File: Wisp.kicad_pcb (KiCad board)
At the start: 4 copper layers, 36 x 36 mm, 38 parts, among them J1 USB4105-GF-A, J2 SM04B-GHS-TB, J3 Conn_01x05_Pin, J4 Conn_01x05_Pin, J5 Conn_01x04_Pin, J6 Conn_01x04_Pin, J9 Conn_02x04_Counter_Clockwise, SW2 PTS810 SJM 250 SMTR LFS, SW3 PTS810 SJM 250 SMTR LFS, U1 ESP32-S3-MINI-1, U2 USBLC6-2SC6, U3 AP2112K-3.3TRG1, U4 TPS7A2033PYCJR, U5 DWM3000TR13

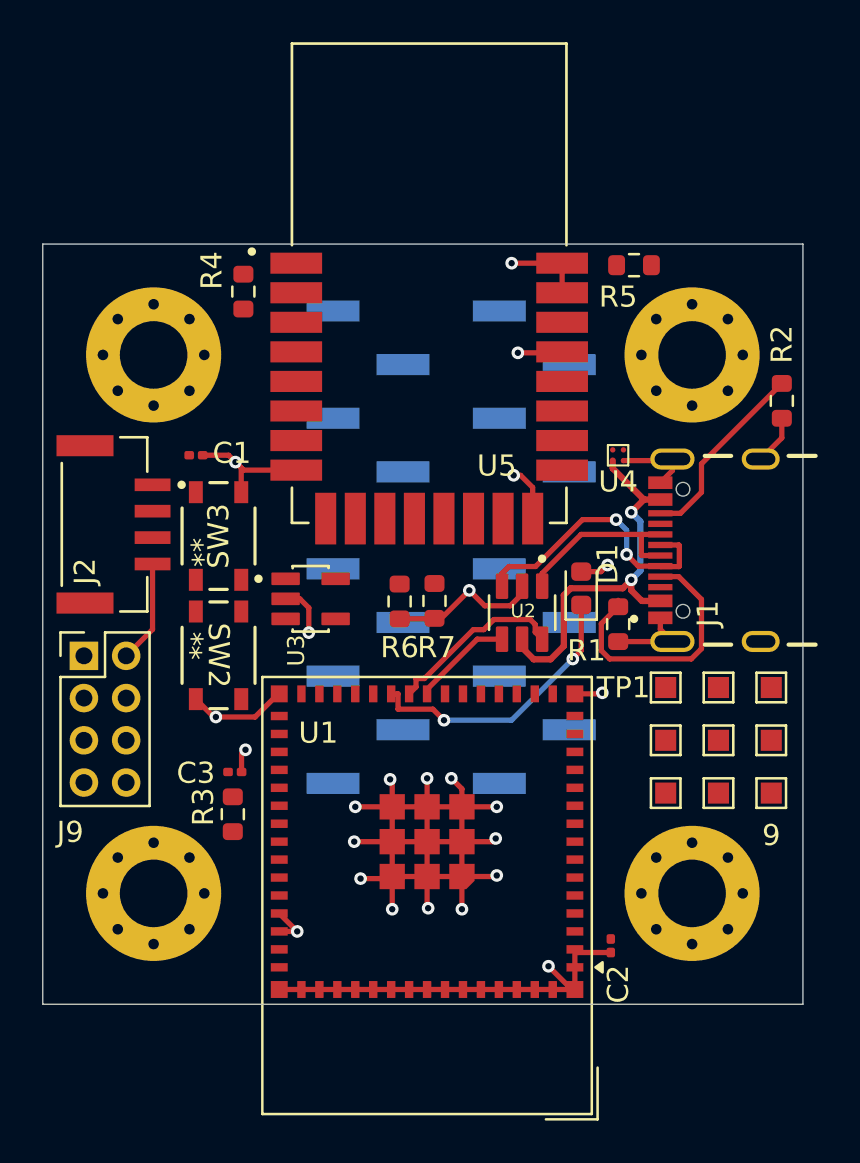
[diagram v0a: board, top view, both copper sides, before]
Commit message: Shifted to a 4 layer board, routed 75% of the traces. DRC needs to run
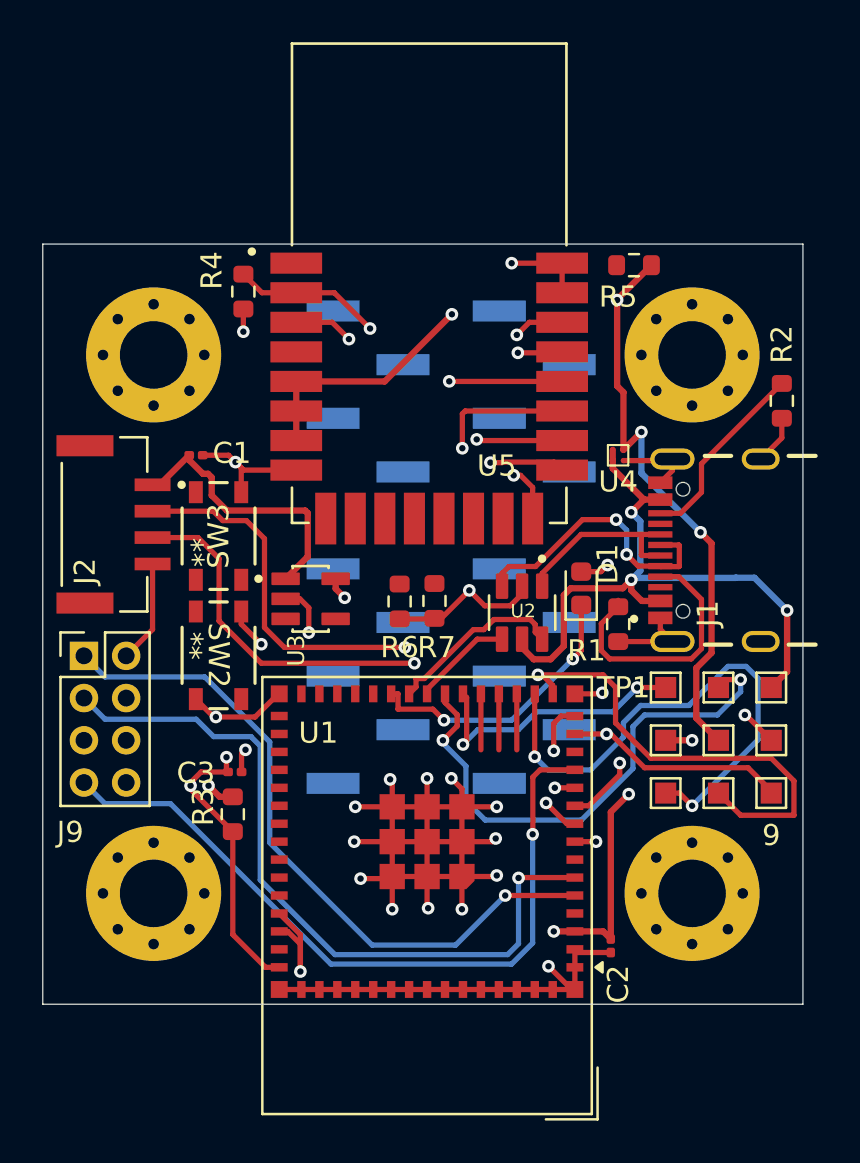
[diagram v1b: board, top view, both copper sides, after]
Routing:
- net +3V3: track 0.00 -> 51.5 mm, vias 0 -> 5
- net /UWB_MISO: track 0.00 -> 50.1 mm, vias 0 -> 3
- net +3V3_UWB: track 0.00 -> 47.0 mm, vias 0 -> 4
- net /FC_RX: track 0.00 -> 46.8 mm, vias 0 -> 3
- net /UWB_SCLK: track 0.00 -> 43.9 mm, vias 0 -> 2
- net /UWB_IRQ: track 0.00 -> 40.8 mm, vias 0 -> 2
- net /UWB_MOSI: track 0.00 -> 37.7 mm, vias 0 -> 3
- net /FC_TX: track 0.00 -> 37.3 mm, vias 0 -> 3
- net /UWB_WAKE: track 0.00 -> 37.1 mm, vias 0 -> 2
- net /DIP_ID1: track 0.00 -> 36.4 mm, vias 0 -> 1
- net /DIP_ID0: track 0.00 -> 35.3 mm, vias 0 -> 1
- net /DIP_ID2: track 0.00 -> 35.2 mm, vias 0 -> 1
- net /DIP_ROLE: track 0.00 -> 32.7 mm, vias 0 -> 1
- net /UWB_RST: track 0.00 -> 32.1 mm, vias 0 -> 2
- net /UWB_CS: track 0.00 -> 31.4 mm, vias 0 -> 2
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
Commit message: Routed miscellaneous traces
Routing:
- net /IO42: track 0.00 -> 38.6 mm, vias 0 -> 1
- net /IO41: track 0.00 -> 27.7 mm, vias 0 -> 2
- net /BTN_CAL: track 0.00 -> 23.7 mm, vias 0 -> 2
- net /IO16: track 2.65 -> 24.4 mm
- net /IO48: track 0.00 -> 18.1 mm, vias 0 -> 1
- net /IO47: track 0.00 -> 16.5 mm, vias 0 -> 1
- net /IO26: track 0.00 -> 11.9 mm, vias 0 -> 1
- net /UWB_CS: track 31.4 -> 42.7 mm
- net /UWB_MOSI: track 37.7 -> 40.8 mm
- net /IO15: track 2.65 -> 0.00 mm
- net /IO14: track 2.65 -> 0.00 mm
- net /FC_TX: track 37.3 -> 36.3 mm
- net /UWB_MISO: track 50.1 -> 49.5 mm

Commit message: Completed V1.0
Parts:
- removed J3, J4: Conn_01x05_Pin, Connector_PinHeader_2.54mm:PinHeader_1x05_P2.54mm_Vertical_SMD_Pin1Right
- removed J5: Conn_01x04_Pin, Connector_PinHeader_2.54mm:PinHeader_1x04_P2.54mm_Vertical_SMD_Pin1Right
- added G***: LOGO, wisp-daughter-board:TL Logo, B.Cu at (129.1, 120.6)
- renumbered TP1 to 1
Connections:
- U1 pad 18: /IO14 -> unconnected-(U1-IO14-Pad18)
- U1 pad 19: /IO15 -> unconnected-(U1-IO15-Pad19)
- U1 pad 20: /IO16 -> unconnected-(U1-IO16-Pad20)
- U1 pad 26: /IO26 -> unconnected-(U1-IO26-Pad26)
- U1 pad 28: /IO33 -> unconnected-(U1-IO33-Pad28)
- U1 pad 29: /IO34 -> unconnected-(U1-IO34-Pad29)
- U1 pad 31: /IO35 -> unconnected-(U1-IO35-Pad31)
- U1 pad 32: /IO36 -> unconnected-(U1-IO36-Pad32)
- U1 pad 33: /IO37 -> unconnected-(U1-IO37-Pad33)
- U1 pad 34: /IO38 -> unconnected-(U1-IO38-Pad34)
- U1 pad 35: /IO39 -> unconnected-(U1-IO39-Pad35)
- U1 pad 36: /IO40 -> unconnected-(U1-IO40-Pad36)
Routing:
- net /IO16: track 24.4 -> 0.00 mm
- net +5V: track 44.4 -> 68.7 mm, vias 3 -> 4
- net /IO26: track 11.9 -> 0.00 mm, vias 1 -> 0
- net GND: track 112.8 -> 111.5 mm
- net /UWB_MISO: track 49.5 -> 48.4 mm
- net /EN: track 21.6 -> 21.3 mm, vias 3 -> 2
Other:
- board text added: "Wisp Daughter Board V1.0"

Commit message: Fixed bugs
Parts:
- removed R6, R7: 10k, Resistor_SMD:R_0603_1608Metric
- added C4: 1uF, Capacitor_SMD:C_0603_1608Metric, F.Cu at (119.7, 108.9)
- added C5: 10uF, Capacitor_SMD:C_0603_1608Metric, F.Cu at (137.4, 112.5)
- added C6: 1uF, Capacitor_SMD:C_0603_1608Metric, F.Cu at (111.1, 109.2)
- C1: footprint Capacitor_SMD:C_0201_0603Metric -> Capacitor_SMD:C_0603_1608Metric
- C2: value 22u -> 22uF; footprint Capacitor_SMD:C_0201_0603Metric -> Capacitor_SMD:C_0603_1608Metric
- C3: value 1u -> 1uF; footprint Capacitor_SMD:C_0201_0603Metric -> Capacitor_SMD:C_0603_1608Metric
- U4: value TPS7A2033PYCJR -> TPS7A2033PDBVR; footprint TPS7A2033PYCJR:TPS7A2033PYCJR -> TPS7A2033PDBVR:SOT95P280X145-5N
- moved U4 12.1 mm to (127.5, 119.1), turned to 180 degrees
- moved C1 0.97 mm to (118.2, 112.0)
- moved C2 0.93 mm to (137.0, 136.2)
- moved R3 0.90 mm to (119.3, 129.8)
- moved C3 0.81 mm to (118.3, 126.9)
- turned D1 to -90 degrees
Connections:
- D1 pad 1: /LED_STATUS -> GND
- D1 pad 2: GND -> /LED_STATUS
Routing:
- net +3V3_UWB: track 47.0 -> 74.0 mm, vias 4 -> 7
- net +3V3: track 51.5 -> 70.7 mm, vias 5 -> 6
- net /EN: track 21.3 -> 29.9 mm, vias 2 -> 3
- net +5V: track 68.7 -> 72.7 mm
- net GND: track 111.5 -> 112.1 mm, vias 25 -> 26
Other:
- board text removed: "9"
